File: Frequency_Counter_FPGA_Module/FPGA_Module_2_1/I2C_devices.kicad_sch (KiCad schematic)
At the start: 50 parts, among them J6 CLK_OUT_1, J7 CLK_OUT_2, U10 TMP117xxDRV, U11 TMP117xxDRV, U12 AD5693RxRM, U8 ADS1115, U9 SI5356A

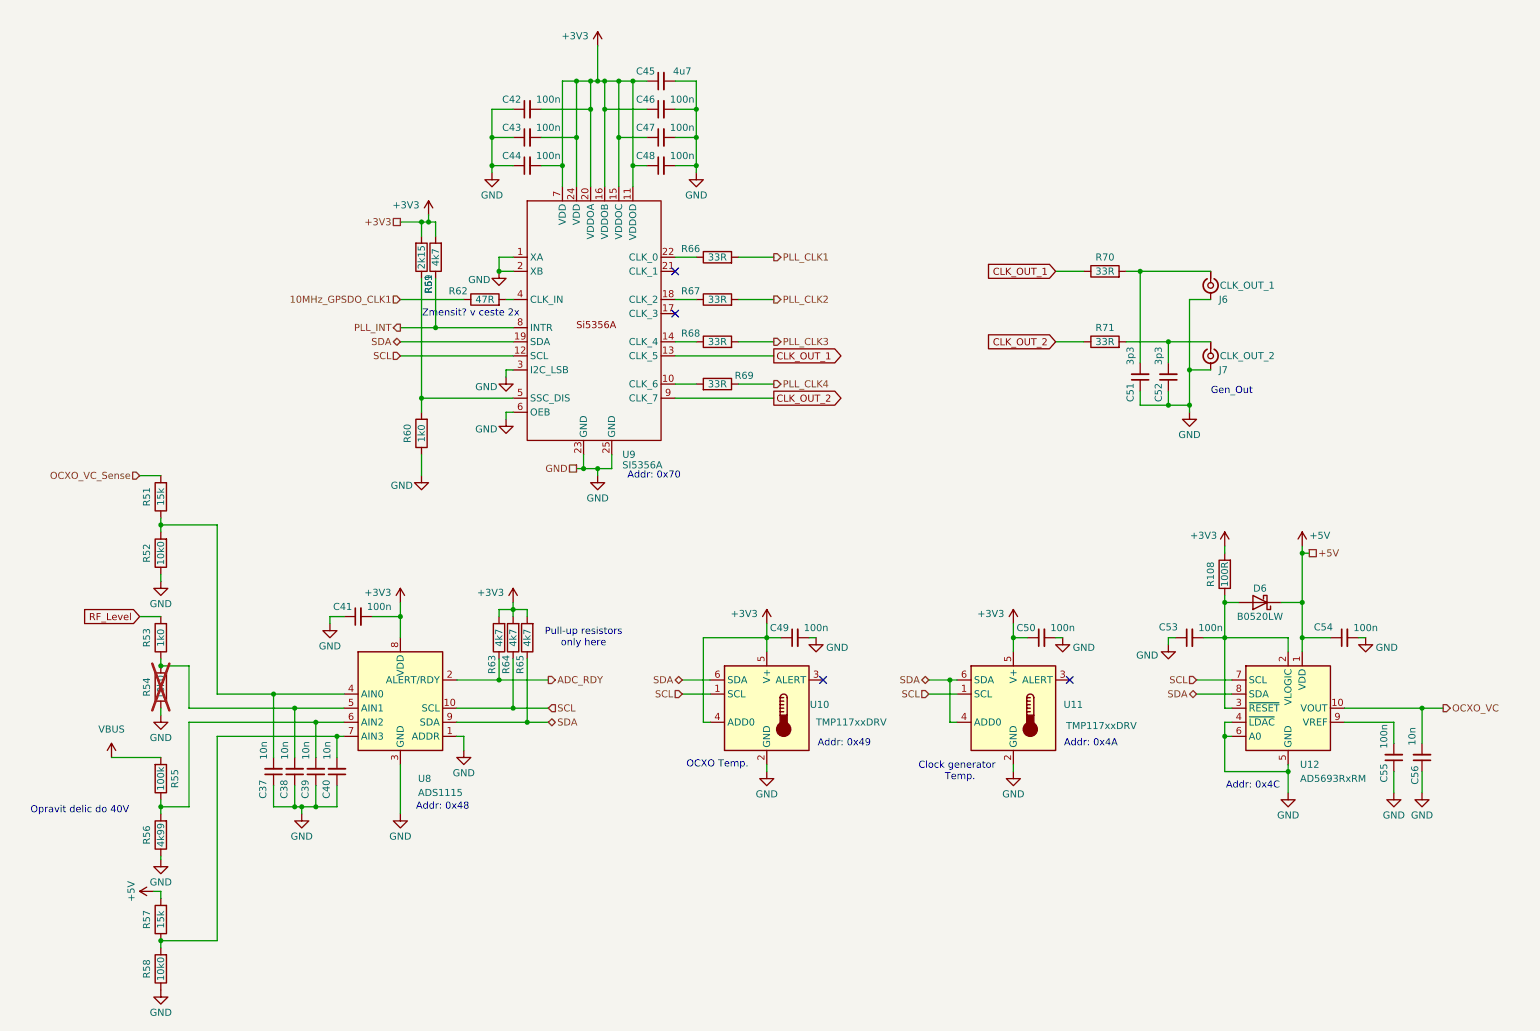
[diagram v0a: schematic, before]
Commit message: chore(hw): KiCad nosne desky FPGA 2.0 -> 2.1 (vc. Gerberu)
Zalohy KiCadu (FPGA_module-backups/, *-bak) ignoruje .gitignore.

Co-Authored-By: Claude Opus 5.5 <noreply@anthropic.com>
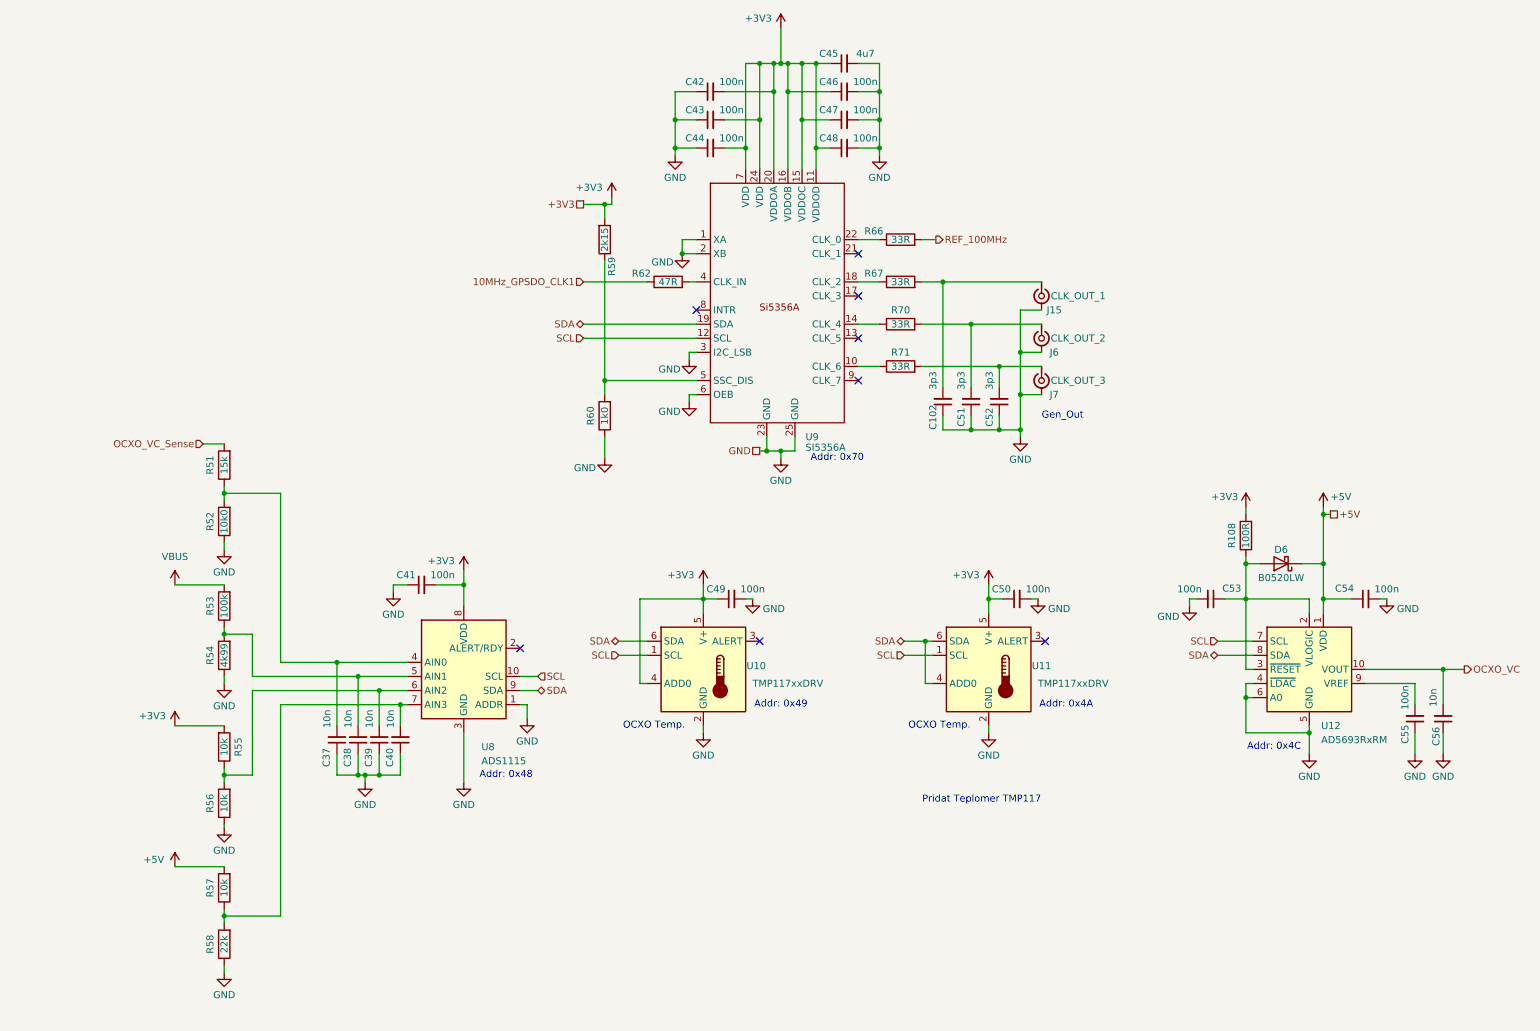
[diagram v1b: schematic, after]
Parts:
- removed R61, R63, R64, R65: 4k7, Resistor_SMD:R_0805_2012Metric, symbol Device:R
- removed R68, R69: 33R, Resistor_SMD:R_0805_2012Metric, symbol Device:R
- added C102: 3p3, Capacitor_SMD:C_0805_2012Metric, symbol Device:C_Small
- added J15: CLK_OUT_1, Connector_Coaxial:U.FL_Hirose_U.FL-R-SMT-1_Vertical, symbol Connector:Conn_Coaxial_Small
- J6: value CLK_OUT_1 -> CLK_OUT_2
- J7: value CLK_OUT_2 -> CLK_OUT_3
- R53: value 1k0 -> 100k
- R54: value 10k0 -> 4k99; now fitted
- R55: value 100k -> 10k
- R56: value 4k99 -> 10k
- R57: value 15k -> 10k
- R58: value 10k0 -> 22k; LCSC link https://www.lcsc.com/product-detail/Chip-Resistor-Surface-M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 -> (none)
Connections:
- net RF_Level is gone; now on net VBUS: R53.2
- net +3V3: now also R55.2
- net GND: now also C53.2, C102.1, J15.2 (Ext); no longer C53.1
- net VBUS: no longer R55.2
- net at D6.2 (A), R108.1, U12.2 (VLOGIC)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: now also C53.1; no longer C53.2
- net at U9.14 (CLK_4): now also R70.1
- net at U9.10 (CLK_6): now also R71.1
- net ADC_RDY: no longer names the net of U8.2 (ALERT/RDY)
- net CLK_OUT_1: no longer names the net of U9.13 (CLK_5)
- net CLK_OUT_1: no longer R70.1
- net CLK_OUT_2: no longer names the net of U9.9 (CLK_7)
- net CLK_OUT_2: no longer R71.1
- net PLL_CLK1 renamed REF_100MHz
- net PLL_CLK2: no longer names the net of R67.2
- net PLL_CLK2: now also C102.2, J15.1 (In)
- net PLL_INT: no longer names the net of U9.8 (INTR)
- no-connect marks 4 -> 8
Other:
- note added: "Pridat Teplomer TMP117"
- note removed: "Clock generator Temp."
- note removed: "Opravit delic do 40V"
- note removed: "Pull-up resistors only here"
- note removed: "Zmensit? v ceste 2x"
- moved on the sheet: C37, C38, C39, C40, C41, C42, C43, C44, C45, C46, C47, C48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
